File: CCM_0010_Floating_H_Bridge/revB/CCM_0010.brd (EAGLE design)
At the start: 31.8 x 63.5 mm, 36 parts, among them IC1 ADUM5230, IC2 L78L12, IC3 HIP4080A, X1 22-23-2021, X2 22-23-2021, X3 22-23-2041, X4 22-23-2041

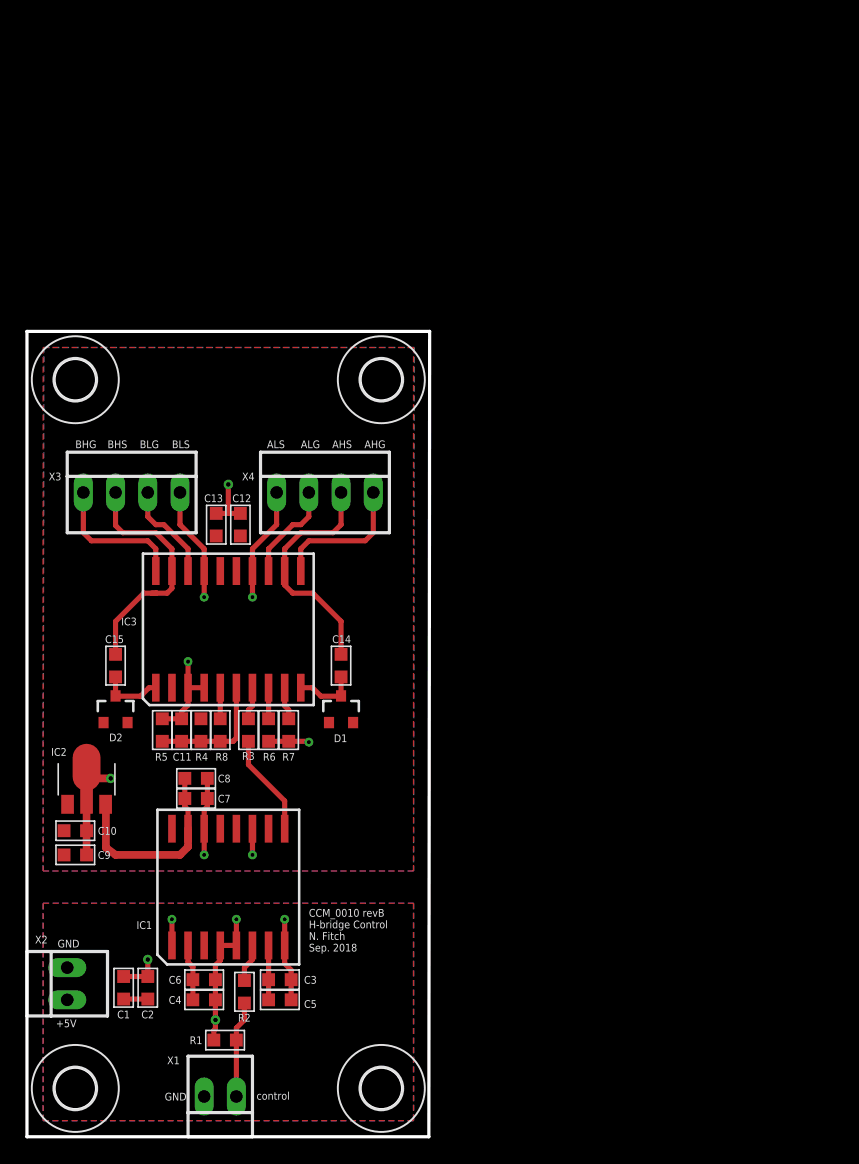
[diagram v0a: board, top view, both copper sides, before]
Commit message: Finalized design of revB of CCM_0010.  Floating H-bridge now uses a lower power driver, makes it possible to monitor the coil current, and implements an optically isolated bypass option.  This latter feature allows either the top or bottom MOT coils to be bypasses, greatly improving flexibility, while simultaneously eliminated ground loop problems with the bypass control signal.
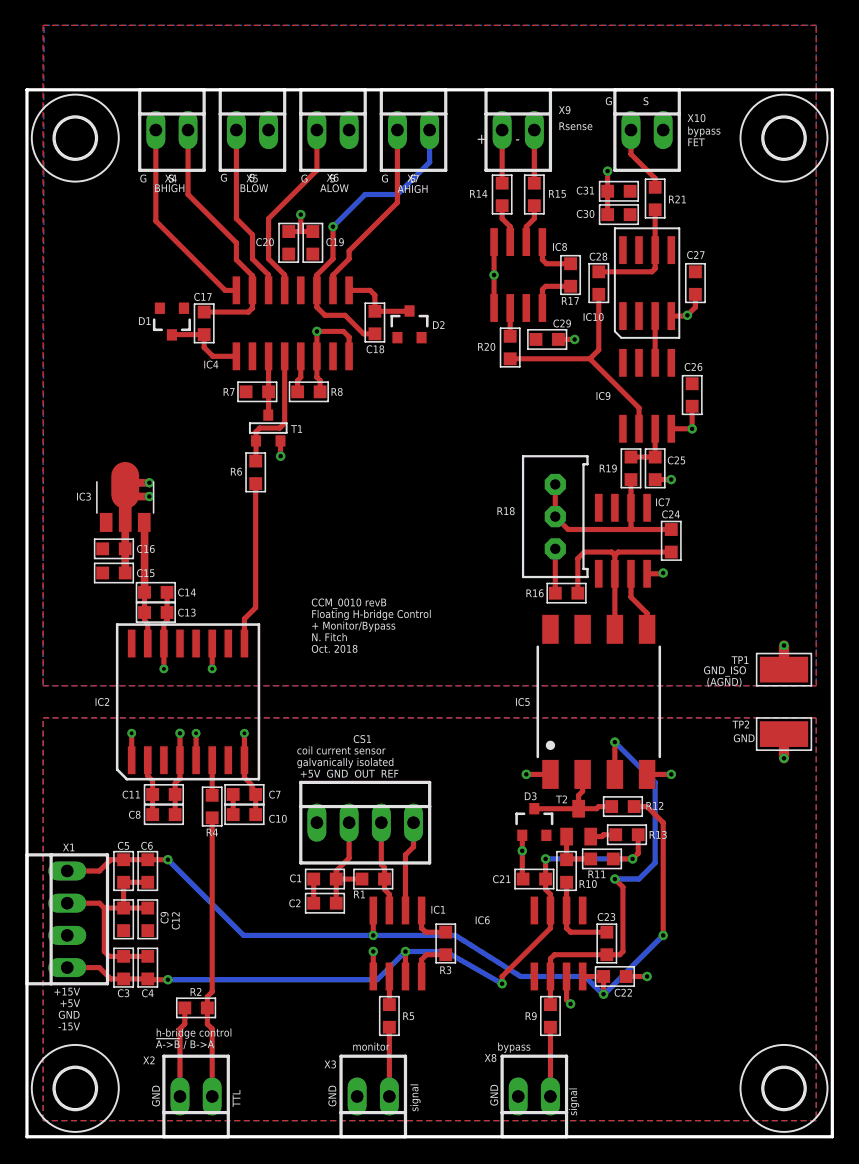
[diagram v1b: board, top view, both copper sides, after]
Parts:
- added C16, C20, C31: 4.7u, acrooptics:0603
- added C17, C18, C19, C21, C22, C26, C27, C29, C30: 0.1u, acrooptics:0603
- added C23: 47p, acrooptics:0603
- added C24, C28: 22p, acrooptics:0603
- added C25: DNI, acrooptics:0603
- added CS1: CASR15X, noah:22-23-2041
- added D3: BAS70, WCSMain:SOT23-3
- added IC10: BUF634, noah:SO8
- added IC4: HIP4082, noah:SO16
- added IC5: HCNR200-300E, avago:DIP8-400
- added IC6: OP97, analog-devices:SO8
- added IC7, IC9: AD820R, analog-devices:SO8
- added IC8: AD8227, analog-devices:SO8
- added R10: 6.8k, acrooptics:0603
- added R11: 2.2k, acrooptics:0603
- added R12: 33k, acrooptics:0603
- added R13: 270, acrooptics:0603
- added R14, R15, R19, R20: 1k, acrooptics:0603
- added R16: 90k, acrooptics:0603
- added R17: 842, acrooptics:0603
- added R18: 20k, bourns:3386W
- added R21: 100, acrooptics:0603
- added R9: 100k, acrooptics:0603
- added T1: 2N7002, zetex:SOT-23
- added T2: MMBT3906, transistor:SOT23-BEC
- added TP1, TP2: TESTPOINT, noah:TESTPOINT
- added X10, X5, X6, X7, X8, X9: 22-23-2021, con-molex:22-23-2021
- C10, C13, C4: value 4.7u -> 0.1u
- C14, C5, C7, C9: value 0.1u -> 4.7u
- D1, D2: value BAV99 -> BAS70
- IC1: value ADUM5230 -> AD8226; device noah:SO16W -> analog-devices:SO8
- IC2: value L78L12 -> ADUM5230; device linear:SOT89 -> noah:SO16W
- IC3: value HIP4080A -> UAL78L12; device noah:SO20W -> linear:SOT89
- R2: value 100 -> 10k
- R3: value 100 -> 20k
- R4: value 10k -> 100
- R5: value 10k -> 1k
- R6: value 100k -> 100
- R7: value 100k -> 10k
- X1: value 22-23-2021 -> 22-23-2041; device con-molex:22-23-2021 -> con-molex:22-23-2041
- X3, X4: value 22-23-2041 -> 22-23-2021; device con-molex:22-23-2041 -> con-molex:22-23-2021
- moved X3 51.3 mm to (27.3, 3.17), turned to 180 degrees
- moved D2 38.2 mm to (30.2, 64.0)
- moved H4 37.0 mm to (59.7, 78.7)
- moved D1 33.4 mm to (11.4, 64.3), turned to 180 degrees
- moved C12 32.0 mm to (9.53, 17.1)
- moved H2 31.7 mm to (59.7, 3.81)
- moved X4 31.0 mm to (11.4, 79.4)
- moved R5 28.8 mm to (28.6, 9.53), turned to 270 degrees
- moved R8 27.6 mm to (22.2, 58.7), turned to 180 degrees
- moved R7 26.8 mm to (18.2, 58.7), turned to 0 degrees
- moved R3 22.9 mm to (33.0, 15.2)
- moved R6 20.3 mm to (18.0, 52.4)
- moved H3 19.0 mm to (3.81, 78.7)
- moved X1 18.5 mm to (3.17, 17.1), turned to 90 degrees
- moved C1 18.0 mm to (23.5, 20.3), turned to 0 degrees
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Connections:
- removed net A_HIGH_GATE: IC3.11, X4.4
- removed net A_HIGH_SOURCE: C14.1, IC3.12, X4.3
- removed net A_LOW_GATE: IC3.13, X4.2
- removed net A_LOW_SOURCE: IC3.14, X4.1
- removed net B_HIGH_GATE: IC3.20, X3.1
- removed net B_HIGH_SOURCE: C15.1, IC3.19, X3.2
- removed net B_LOW_GATE: IC3.18, X3.3
- removed net B_LOW_SOURCE: IC3.17, X3.4
- new net +15V: C21.2, C3.1, C4.1, IC1.7, IC6.7, R11.2, R13.2, X1.1
- new net -15V: C22.1, C5.2, C6.2, IC1.4, IC6.4, R12.1, X1.4
- new net N$11: R16.2, R18.1
- new net N$12: C23.1, IC6.6, R10.1
- new net N$14: R10.2, R11.1, T2.B
- new net N$15: R13.1, T2.E
- new net N$18: C24.2, IC5.6, IC7.2, R16.1
- new net N$19: IC5.5, IC7.3
- new net N$21: IC4.3, R7.2, T1.1
- new net N$22: IC4.4, R6.2, T1.3
- new net N$25: IC10.3, IC9.6
- new net N$26: C28.1, IC10.6, R21.1
- new net N$27: R21.2, X10.1
- new net N$3: D3.3, IC5.2, R12.2, T2.C
- new net N$31: C28.2, IC9.2, R20.2
- new net N$32: IC4.13, X6.1
- new net N$33: IC4.10, X7.1
- new net N$34: IC1.6, R5.1
- new net N$35: IC1.1, R3.2
- new net N$36: IC1.8, R3.1
- new net N$37: CS1.3, IC1.3, R1.2
- new net N$38: CS1.4, IC1.2
- new net N$39: R5.2, X3.1
- new net N$4: C24.1, IC7.6, R18.2, R18.3, R19.1
- new net N$40: IC8.6, R20.1
- new net N$41: IC8.1, R17.2
- new net N$42: IC8.8, R17.1
- new net N$43: C25.1, IC9.3, R19.2
- new net N$44: R14.1, X9.1
- new net N$45: R15.1, X9.2
- new net N$46: IC8.2, R15.2
- new net N$47: IC8.3, R14.2
- new net N$7: R9.1, X8.1
- new net N$9: C23.2, IC5.3, IC6.2, R9.2
- net +12V: now also C15.1, C16.1, C19.1, C20.1, C26.1, C27.1, C29.1, C30.1, C31.1, IC10.7, IC2.10, IC3.1, IC4.12, IC4.2, IC4.7, IC7.7, IC8.7, IC9.7, R7.1; no longer C10.1, C12.1, C13.1, C9.1, IC1.10, IC2.1, IC3.15, IC3.16, IC3.2, R4.1
- net +5V: now also C10.2, C11.1, C12.1, C7.2, C8.1, C9.1, CS1.1, IC2.2, IC2.7, X1.2; no longer C3.2, C4.1, C5.2, C6.1, IC1.2, IC1.7, X2.1
- net AGND: now also C14.2, C15.2, C16.2, C19.2, C20.2, C25.2, C26.2, C27.2, C29.2, C30.2, C31.2, IC10.4, IC2.11, IC2.14, IC3.2, IC3.2@1, IC4.6, IC4.8, IC7.4, IC8.4, IC8.5, IC9.4, R8.1, T1.2, TP1.P$1, X10.2, X5.2, X6.2; no longer C10.2, C11.2, C12.2, C7.2, C8.2, C9.2, IC1.11, IC1.14, IC2.2, IC2.2@1, IC3.3, IC3.4, R5.2, R6.1, R7.1
- net GND: now also C10.1, C11.2, C12.2, C21.1, C22.2, C3.2, C6.1, C7.1, C8.2, C9.2, CS1.2, D3.1, IC2.1, IC2.4, IC2.5, IC2.8, IC5.1, IC5.4, IC6.3, R2.1, TP2.P$1, X1.3, X3.2, X8.2; no longer C3.1, C6.2, IC1.1, IC1.4, IC1.8, X1.2
- net N$10: now also C13.1, C14.1, IC2.15, IC3.3; no longer C7.1, C8.1, IC1.15, IC2.3
- net N$13: now also IC2.9, R6.1; no longer IC3.7, R3.2
- net N$16: now also C18.2, IC4.11, X7.2; no longer IC3.9, R7.2
- net N$17: now also C17.2, D1.3, IC4.1; no longer C15.2, D2.3, IC3.1
- net N$20: now also C18.1, D2.3, IC4.9; no longer IC3.5, R8.2
- net N$23: now also C17.1, IC4.15, X4.2; no longer C14.2, D1.3, IC3.10
- net N$24: now also IC4.16, X4.1; no longer IC3.8, R6.2
- net N$28: now also R2.2, R4.1, X2.1; no longer R1.2, R2.1, X1.1
- net N$29: now also IC4.14, X5.1; no longer C11.1, IC3.6, R4.2, R5.1, R8.1
- net N$30: now also IC2.6, R4.2; no longer IC1.6, R2.2
- net N$8: now also IC4.5, R8.2; no longer IC1.9, R3.1
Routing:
- net -15V: track 0.00 -> 70.1 mm, vias 0 -> 4
- net +15V: track 0.00 -> 60.3 mm, vias 0 -> 5
- net GND: track 22.9 -> 66.1 mm, vias 5 -> 11
- net N$9: track 0.00 -> 32.6 mm, vias 0 -> 2
- net AGND: track 32.3 -> 55.8 mm, vias 6 -> 15
- net N$16: track 2.58 -> 24.6 mm, vias 0 -> 1
- net B_HIGH_SOURCE: track 19.4 -> 0.00 mm
- net A_HIGH_SOURCE: track 18.9 -> 0.00 mm
- net N$31: track 0.00 -> 18.8 mm
- net N$18: track 0.00 -> 16.4 mm
- net N$4: track 0.00 -> 16.1 mm
- net N$23: track 4.96 -> 20.1 mm
- net N$33: track 0.00 -> 14.7 mm
- net N$32: track 0.00 -> 14.7 mm
- net N$28: track 7.63 -> 22.3 mm
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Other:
- board size 31.8 x 63.5 mm -> 63.5 x 82.5 mm
- board text added: "+ -"
- board text added: "+15V +5V GND -15V"
- board text added: "AHIGH"
- board text added: "ALOW"
- board text added: "BHIGH"
- board text added: "BLOW"
- board text added: "CCM_0010 revB Floating H-bridge Control + Monitor/Bypass N. Fitch Oct. 2018"
- board text added: "G S"
- board text added: "GND_ISO (AGND)"
- board text added: "Rsense"
- board text added: "TTL"
- board text added: "bypass"
- board text added: "bypass FET"
- board text added: "coil current sensor galvanically isolated +5V GND OUT REF"
- board text added: "h-bridge control !A->B! / B->A"
- board text added: "monitor"
- board text added: "signal"
- board text removed: "+5V"
- board text removed: "AHG"
- board text removed: "AHS"
- board text removed: "ALG"
- board text removed: "ALS"
- board text removed: "BHG"
- board text removed: "BHS"
- board text removed: "BLG"
- board text removed: "BLS"
- board text removed: "CCM_0010 revB H-bridge Control N. Fitch Sep. 2018"
- board text removed: "control"
